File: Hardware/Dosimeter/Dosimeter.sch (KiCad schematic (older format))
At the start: 45 parts, among them J1 USB_B_Mini, J2 Vin +12, J3 Conn_01x01_Female, J4 Conn_01x01_Female, J5 Conn_01x02_Male, J6 Conn_01x02_Male, J7 Conn_01x01_Female, J8 Conn_01x04_Male, Q1 BC846, SW1 SW_Push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

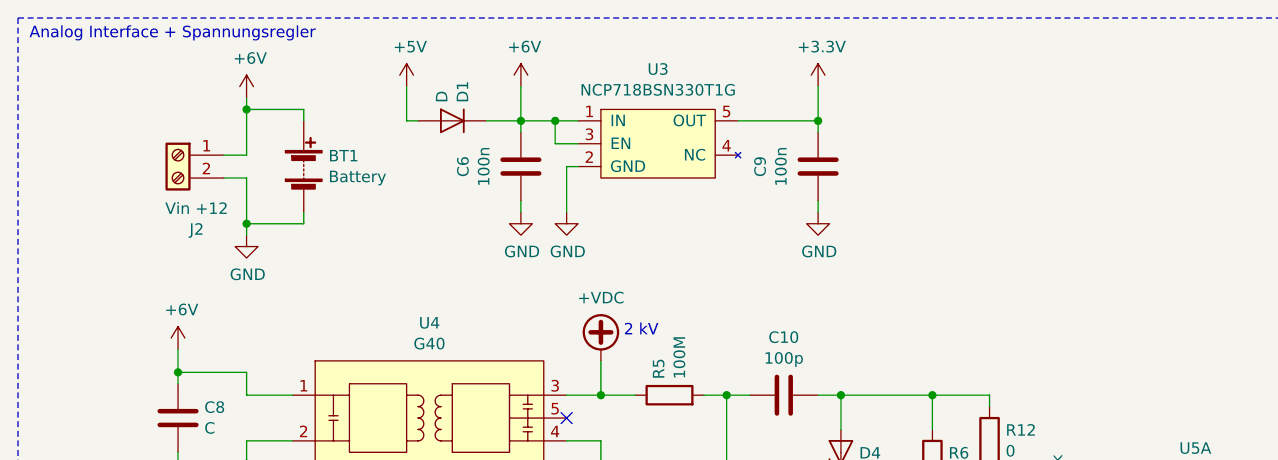
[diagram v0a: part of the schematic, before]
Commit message: update hardware (add switch)
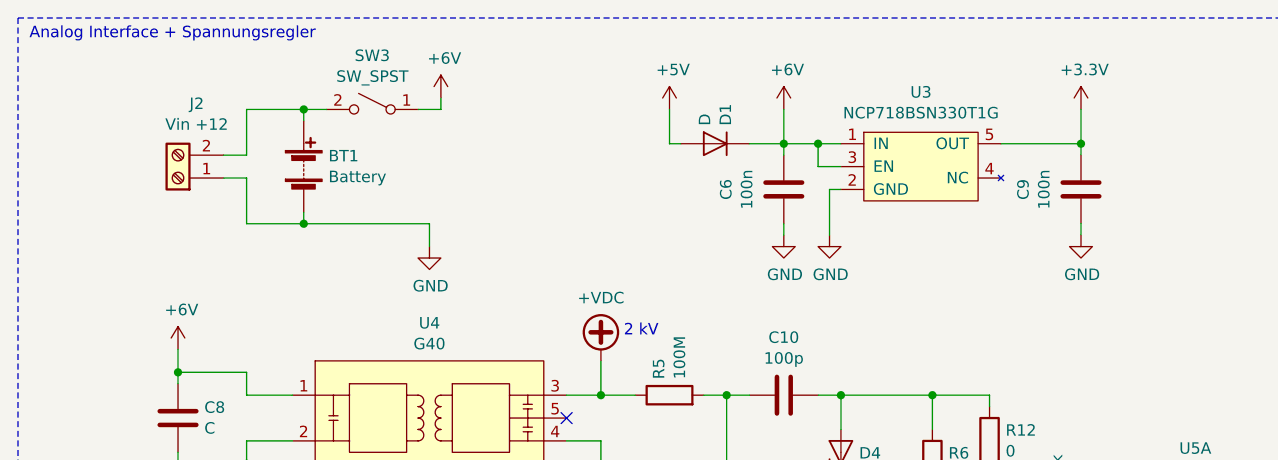
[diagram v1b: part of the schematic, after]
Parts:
- added SW3: SW_SPST, Button_Switch_SMD:SW_SPDT_PCM12, symbol Switch:SW_SPST
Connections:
- net +6V: now also SW3.1 (A); no longer BT1.1 (+), J2.1 (Pin_1)
- net GND: now also J2.1 (Pin_1); no longer J2.2 (Pin_2)
- new net: BT1.1 (+), J2.2 (Pin_2), SW3.2 (B)
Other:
- moved on the sheet: C6, C9, D1, U3
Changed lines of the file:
@@
 L Device:C C6
 U 1 1 5F4657F1
-P 2900 1250
-F 0 "C6" V 2648 1250 50  0000 C CNN
-F 1 "100n" V 2739 1250 50  0000 C CNN
-F 2 "Capacitor_SMD:C_0603_1608Metric" H 2938 1100 50  0001 C CNN
-F 3 "~" H 2900 1250 50  0001 C CNN
-	1    2900 1250
+P 4050 1350
+F 0 "C6" V 3798 1350 50  0000 C CNN
+F 1 "100n" V 3889 1350 50  0000 C CNN
+F 2 "Capacitor_SMD:C_0603_1608Metric" H 4088 1200 50  0001 C CNN
+F 3 "~" H 4050 1350 50  0001 C CNN
+	1    4050 1350
 	1    0    0    -1
 $EndComp
@@
 L Device:C C9
 U 1 1 5F4666EF
-P 4200 1250
-F 0 "C9" V 3948 1250 50  0000 C CNN
-F 1 "100n" V 4039 1250 50  0000 C CNN
-F 2 "Capacitor_SMD:C_0603_1608Metric" H 4238 1100 50  0001 C CNN
-F 3 "~" H 4200 1250 50  0001 C CNN
-	1    4200 1250
-	1    0    0    -1
-$EndComp
-Wire Wire Line
-	2900 1050 2900 1100
-Wire Wire Line
-	4200 1050 4200 1100
+P 5350 1350
+F 0 "C9" V 5098 1350 50  0000 C CNN
+F 1 "100n" V 5189 1350 50  0000 C CNN
+F 2 "Capacitor_SMD:C_0603_1608Metric" H 5388 1200 50  0001 C CNN
+F 3 "~" H 5350 1350 50  0001 C CNN
+	1    5350 1350
+	1    0    0    -1
+$EndComp
+Wire Wire Line
+	4050 1150 4050 1200
+Wire Wire Line
+	5350 1150 5350 1200
 $Comp
 L MK_Supply:NCP718BSN330T1G U3
 U 1 1 5F46C172
-P 3500 1150
-F 0 "U3" H 3500 1475 50  0000 C CNN
-F 1 "NCP718BSN330T1G" H 3500 1384 50  0000 C CNN
-F 2 "Package_TO_SOT_SMD:TSOT-23-5" H 3250 1150 50  0001 C CNN
-F 3 "https://www.mouser.ch/datasheet/2/308/NCP718-D-1224359.pdf" H 3250 1150 50  0001 C CNN
-F 4 "863-NCP718BSN330T1G" H 3500 1150 50  0001 C CNN "Mouser Nr."
-F 5 "NCP718BSN330T1G" H 3500 1150 50  0001 C CNN "Hersteller Nr."
-	1    3500 1150
-	1    0    0    -1
-$EndComp
-Wire Wire Line
-	2900 1050 3050 1050
-Wire Wire Line
-	3150 1150 3050 1150
-Wire Wire Line
-	3050 1150 3050 1050
-Connection ~ 3050 1050
-Wire Wire Line
-	3050 1050 3150 1050
-Wire Wire Line
-	3850 1050 4200 1050
+P 4650 1250
+F 0 "U3" H 4650 1575 50  0000 C CNN
+F 1 "NCP718BSN330T1G" H 4650 1484 50  0000 C CNN
+F 2 "Package_TO_SOT_SMD:TSOT-23-5" H 4400 1250 50  0001 C CNN
+F 3 "https://www.mouser.ch/datasheet/2/308/NCP718-D-1224359.pdf" H 4400 1250 50  0001 C CNN
+F 4 "863-NCP718BSN330T1G" H 4650 1250 50  0001 C CNN "Mouser Nr."
+F 5 "NCP718BSN330T1G" H 4650 1250 50  0001 C CNN "Hersteller Nr."
+	1    4650 1250
+	1    0    0    -1
+$EndComp
+Wire Wire Line
+	4050 1150 4200 1150
+Wire Wire Line
+	4300 1250 4200 1250
+Wire Wire Line
+	4200 1250 4200 1150
+Connection ~ 4200 1150
+Wire Wire Line
+	4200 1150 4300 1150
+Wire Wire Line
+	5000 1150 5350 1150
 $Comp
 L power:GND #PWR0117
 U 1 1 5F4760F4
-P 3100 1450
-F 0 "#PWR0117" H 3100 1200 50  0001 C CNN
-F 1 "GND" H 3105 1277 50  0000 C CNN
-F 2 "" H 3100 1450 50  0001 C CNN
-F 3 "" H 3100 1450 50  0001 C CNN
-	1    3100 1450
-	1    0    0    -1
-$EndComp
-Wire Wire Line
-	3100 1450 3100 1250
-Wire Wire Line
-	3100 1250 3150 1250
+P 4250 1550
+F 0 "#PWR0117" H 4250 1300 50  0001 C CNN
+F 1 "GND" H 4255 1377 50  0000 C CNN
+F 2 "" H 4250 1550 50  0001 C CNN
+F 3 "" H 4250 1550 50  0001 C CNN
+	1    4250 1550
+	1    0    0    -1
+$EndComp
+Wire Wire Line
+	4250 1550 4250 1350
+Wire Wire Line
+	4250 1350 4300 1350
 $Comp
 L power:GND #PWR0118
 U 1 1 5F4783D9
-P 2900 1450
-F 0 "#PWR0118" H 2900 1200 50  0001 C CNN
-F 1 "GND" H 2905 1277 50  0000 C CNN
-F 2 "" H 2900 1450 50  0001 C CNN
-F 3 "" H 2900 1450 50  0001 C CNN
-	1    2900 1450
-	1    0    0    -1
-$EndComp
-Wire Wire Line
-	2900 1450 2900 1400
+P 4050 1550
+F 0 "#PWR0118" H 4050 1300 50  0001 C CNN
+F 1 "GND" H 4055 1377 50  0000 C CNN
+F 2 "" H 4050 1550 50  0001 C CNN
+F 3 "" H 4050 1550 50  0001 C CNN
+	1    4050 1550
+	1    0    0    -1
+$EndComp
+Wire Wire Line
+	4050 1550 4050 1500
 $Comp
 L power:GND #PWR0119
 U 1 1 5F47B29D
-P 4200 1450
-F 0 "#PWR0119" H 4200 1200 50  0001 C CNN
-F 1 "GND" H 4205 1277 50  0000 C CNN
-F 2 "" H 4200 1450 50  0001 C CNN
-F 3 "" H 4200 1450 50  0001 C CNN
-	1    4200 1450
-	1    0    0    -1
-$EndComp
-Wire Wire Line
-	4200 1450 4200 1400
+P 5350 1550
+F 0 "#PWR0119" H 5350 1300 50  0001 C CNN
+F 1 "GND" H 5355 1377 50  0000 C CNN
+F 2 "" H 5350 1550 50  0001 C CNN
+F 3 "" H 5350 1550 50  0001 C CNN
+	1    5350 1550
+	1    0    0    -1
+$EndComp
+Wire Wire Line
+	5350 1550 5350 1500
 $Comp
 L power:+3.3V #PWR0120
 U 1 1 5F47DF7C
-P 4200 900
-F 0 "#PWR0120" H 4200 750 50  0001 C CNN
-F 1 "+3.3V" H 4215 1073 50  0000 C CNN
-F 2 "" H 4200 900 50  0001 C CNN
-F 3 "" H 4200 900 50  0001 C CNN
-	1    4200 900
-	1    0    0    -1
-$EndComp
-Wire Wire Line
-	4200 900  4200 1050
-Connection ~ 4200 1050
-Wire Wire Line
-	2900 900  2900 1050
-Connection ~ 2900 1050
+P 5350 1000
+F 0 "#PWR0120" H 5350 850 50  0001 C CNN
+F 1 "+3.3V" H 5365 1173 50  0000 C CNN
+F 2 "" H 5350 1000 50  0001 C CNN
+F 3 "" H 5350 1000 50  0001 C CNN
+	1    5350 1000
+	1    0    0    -1
+$EndComp
+Wire Wire Line
+	5350 1000 5350 1150
+Connection ~ 5350 1150
+Wire Wire Line
+	4050 1000 4050 1150
+Connection ~ 4050 1150
 $Comp
 L Connector:Screw_Terminal_01x02 J2
 U 1 1 5F4859A1
-P 1400 1200
-F 0 "J2" H 1318 875 50  0000 C CNN
-F 1 "Vin +12" H 1318 966 50  0000 C CNN
-F 2 "MK_Footprints:TerminalBlock_Phoenix_MPT-0,5-2-2.54_1x02_P2.54mm_Horizontal" H 1400 1200 50  0001 C CNN
-F 3 "~" H 1400 1200 50  0001 C CNN
-	1    1400 1200
-	-1   0    0    -1
+P 1400 1300
+F 0 "J2" H 1318 975 50  0000 C CNN
+F 1 "Vin +12" H 1318 1066 50  0000 C CNN
+F 2 "MK_Footprints:TerminalBlock_Phoenix_MPT-0,5-2-2.54_1x02_P2.54mm_Horizontal" H 1400 1300 50  0001 C CNN
+F 3 "~" H 1400 1300 50  0001 C CNN
+	1    1400 1300
+	-1   0    0    1
 $EndComp
 Wire Wire Line
@@
 L power:GND #PWR0122
 U 1 1 5F4859A8
-P 1700 1550
-F 0 "#PWR0122" H 1700 1300 50  0001 C CNN
-F 1 "GND" H 1705 1377 50  0000 C CNN
-F 2 "" H 1700 1550 50  0001 C CNN
-F 3 "" H 1700 1550 50  0001 C CNN
-	1    1700 1550
+P 2500 1600
+F 0 "#PWR0122" H 2500 1350 50  0001 C CNN
+F 1 "GND" H 2505 1427 50  0000 C CNN
+F 2 "" H 2500 1600 50  0001 C CNN
+F 3 "" H 2500 1600 50  0001 C CNN
+	1    2500 1600
 	1    0    0    -1
 $EndComp
@@
 	1700 1300 1700 1500
 Wire Wire Line
-	1700 950  1700 1000
+	2550 950  2550 1000
 $Comp
 L Device:C C5
@@
 L Device:D D1
 U 1 1 5F51A8DE
-P 2600 1050
-F 0 "D1" V 2554 1129 50  0000 L CNN
-F 1 "D" V 2645 1129 50  0000 L CNN
-F 2 "Diode_SMD:D_0603_1608Metric" H 2600 1050 50  0001 C CNN
-F 3 "~" H 2600 1050 50  0001 C CNN
-	1    2600 1050
+P 3750 1150
+F 0 "D1" V 3704 1229 50  0000 L CNN
+F 1 "D" V 3795 1229 50  0000 L CNN
+F 2 "Diode_SMD:D_0603_1608Metric" H 3750 1150 50  0001 C CNN
+F 3 "~" H 3750 1150 50  0001 C CNN
+	1    3750 1150
 	-1   0    0    -1
 $EndComp
 Wire Wire Line
-	2750 1050 2900 1050
-Wire Wire Line
-	2450 1050 2400 1050
-Wire Wire Line
-	2400 1050 2400 900
+	3900 1150 4050 1150
+Wire Wire Line
+	3600 1150 3550 1150
+Wire Wire Line
+	3550 1150 3550 1000
 $Comp
 L power:+5V #PWR0132
 U 1 1 5F529DD5
-P 2400 900
-F 0 "#PWR0132" H 2400 750 50  0001 C CNN
-F 1 "+5V" H 2415 1073 50  0000 C CNN
-F 2 "" H 2400 900 50  0001 C CNN
-F 3 "" H 2400 900 50  0001 C CNN
-	1    2400 900
+P 3550 1000
+F 0 "#PWR0132" H 3550 850 50  0001 C CNN
+F 1 "+5V" H 3565 1173 50  0000 C CNN
+F 2 "" H 3550 1000 50  0001 C CNN
+F 3 "" H 3550 1000 50  0001 C CNN
+	1    3550 1000
 	1    0    0    -1
 $EndComp
@@
 L power:+6V #PWR0103
 U 1 1 5F4FAFC7
-P 1700 950
-F 0 "#PWR0103" H 1700 800 50  0001 C CNN
-F 1 "+6V" H 1715 1123 50  0000 C CNN
-F 2 "" H 1700 950 50  0001 C CNN
-F 3 "" H 1700 950 50  0001 C CNN
-	1    1700 950
+P 2550 950
+F 0 "#PWR0103" H 2550 800 50  0001 C CNN
+F 1 "+6V" H 2565 1123 50  0000 C CNN
+F 2 "" H 2550 950 50  0001 C CNN
+F 3 "" H 2550 950 50  0001 C CNN
+	1    2550 950
 	1    0    0    -1
 $EndComp
@@
 L power:+6V #PWR0104
 U 1 1 5F50BFD5
-P 2900 900
-F 0 "#PWR0104" H 2900 750 50  0001 C CNN
-F 1 "+6V" H 2915 1073 50  0000 C CNN
-F 2 "" H 2900 900 50  0001 C CNN
-F 3 "" H 2900 900 50  0001 C CNN
-	1    2900 900
+P 4050 1000
+F 0 "#PWR0104" H 4050 850 50  0001 C CNN
+F 1 "+6V" H 4065 1173 50  0000 C CNN
+F 2 "" H 4050 1000 50  0001 C CNN
+F 3 "" H 4050 1000 50  0001 C CNN
+	1    4050 1000
 	1    0    0    -1
 $EndComp
@@
 Wire Wire Line
 	1950 1000 1700 1000
-Connection ~ 1700 1000
 Wire Wire Line
 	1700 1000 1700 1200
@@
 Wire Wire Line
 	1950 1500 1700 1500
-Connection ~ 1700 1500
-Wire Wire Line
-	1700 1500 1700 1550
 Text GLabel 5950 4950 2    50   BiDi ~ 0
 SWDIO
@@
 	5300 3050 5300 3150
 $Comp
-L power:+6V #PWR?
+L power:+6V #PWR0121
 U 1 1 5F6F4E43
 P 5300 3050
-F 0 "#PWR?" H 5300 2900 50  0001 C CNN
+F 0 "#PWR0121" H 5300 2900 50  0001 C CNN
 F 1 "+6V" H 5315 3223 50  0000 C CNN
 F 2 "" H 5300 3050 50  0001 C CNN
@@
 	1    0    0    -1
 $EndComp
+Wire Wire Line
+	1950 1500 2500 1500
+Wire Wire Line
+	2500 1500 2500 1600
+Connection ~ 1950 1500
+$Comp
+L Switch:SW_SPST SW3
+U 1 1 5F522CE9
+P 2250 1000
+F 0 "SW3" H 2250 1235 50  0000 C CNN
+F 1 "SW_SPST" H 2250 1144 50  0000 C CNN
+F 2 "Button_Switch_SMD:SW_SPDT_PCM12" H 2250 1000 50  0001 C CNN
+F 3 "~" H 2250 1000 50  0001 C CNN
+	1    2250 1000
+	-1   0    0    -1
+$EndComp
+Wire Wire Line
+	2550 1000 2450 1000
+Wire Wire Line
+	2050 1000 1950 1000
+Connection ~ 1950 1000
 $EndSCHEMATC
